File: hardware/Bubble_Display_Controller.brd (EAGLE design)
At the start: 38.1 x 43.2 mm, 33 parts, among them J1 ICSP, Q10 IRFML8244, Q11 IRFML8244, Q12 IRFML8244, Q13 IRFML8244, Q14 IRFML8244, Q15 IRFML8244, Q16 IRFML8244, Q9 IRFML8244, U4 ATMEGA328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

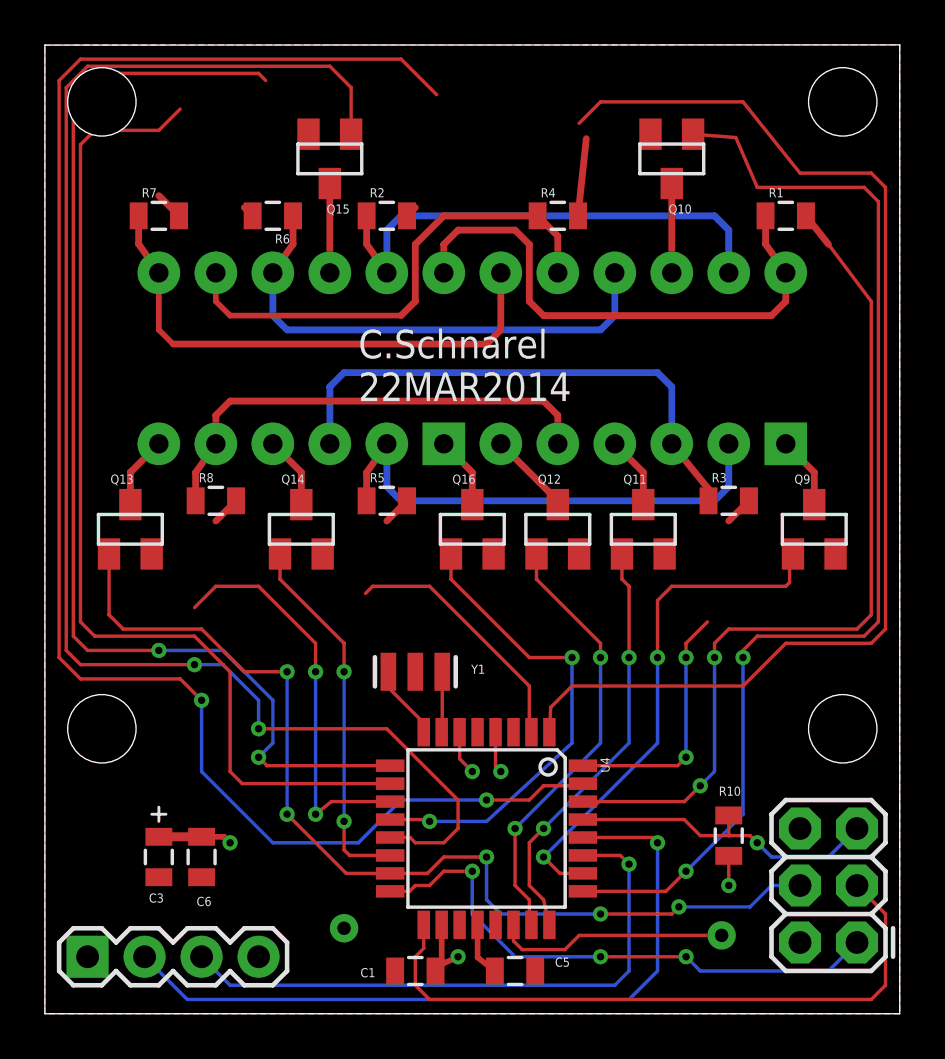
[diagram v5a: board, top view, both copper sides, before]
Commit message: Ordered new board, 8Jyd7Mea. Updating docs to match.
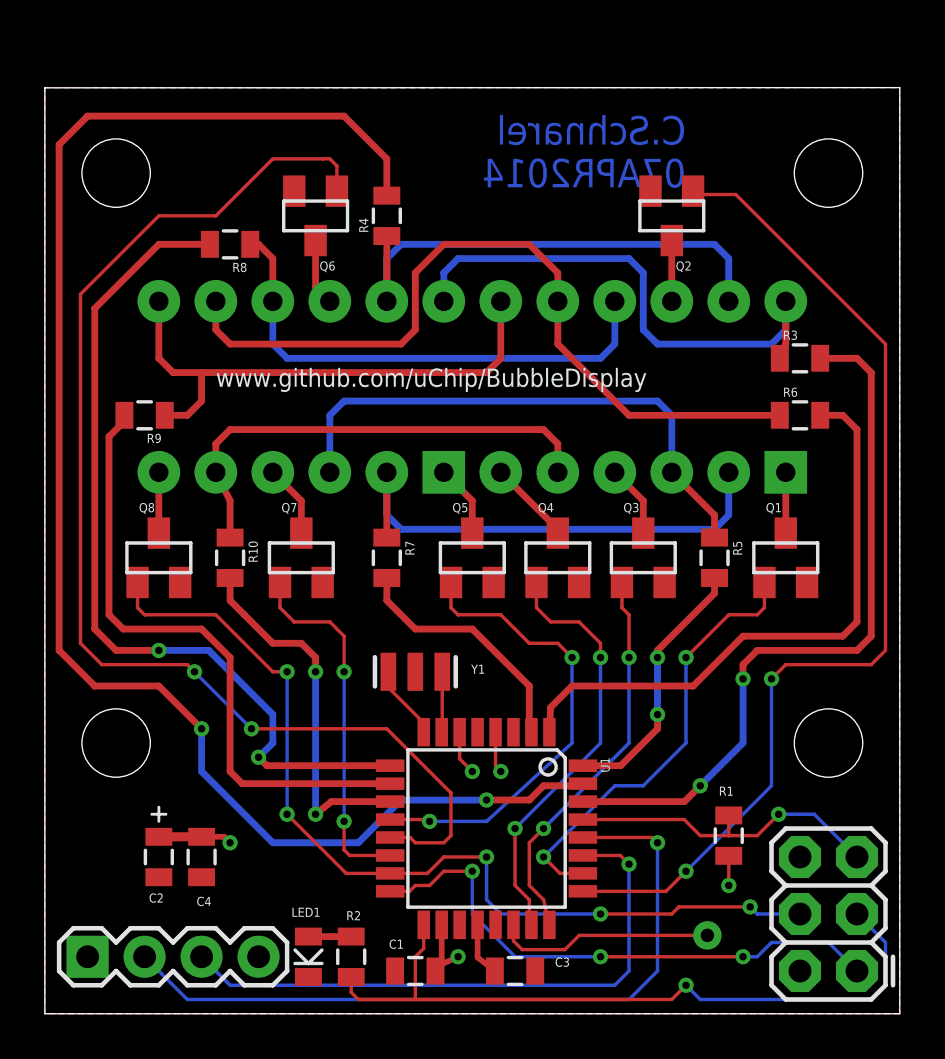
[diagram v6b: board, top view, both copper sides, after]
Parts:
- removed C5: 0.1uF, SparkFun-Capacitors:0805
- removed JP3: BREADBD_VIA, ChipsParts:BBD-VIA
- removed Q10, Q11, Q12, Q13, Q14, Q15, Q16, Q9: IRFML8244, SparkFun-DiscreteSemi:SOT23
- added C2: 10uF, ChipsParts:0805-POL
- added LED1: Amber, ChipsParts:0805-LED
- added Q1, Q2, Q3, Q4, Q5, Q6, Q7, Q8: IRFML8244, SparkFun-DiscreteSemi:SOT23
- added R9: 75, SparkFun-Resistors:0805
- C3: value 10uF -> 0.1uF; device ChipsParts:0805-POL -> SparkFun-Capacitors:0805
- R1: value 75 -> 10k
- R10: value 10k -> 75
- R2: value 75 -> 1k
- moved R2 33.1 mm to (13.7, 2.54), turned to 90 degrees
- moved R1 27.7 mm to (30.5, 7.94), turned to 270 degrees
- moved R10 25.4 mm to (8.26, 20.3)
- moved R6 25.1 mm to (33.7, 26.7), turned to 0 degrees
- moved R7 18.3 mm to (15.2, 20.3), turned to 270 degrees
- moved C3 16.7 mm to (21.0, 1.91), turned to 0 degrees
- moved JP2 16.2 mm to (29.5, 3.49)
- moved R5 14.8 mm to (29.8, 20.3), turned to 270 degrees
- moved R8 11.4 mm to (8.26, 34.3), turned to 180 degrees
- moved R4 7.62 mm to (15.2, 35.6), turned to 90 degrees
- moved R3 7.10 mm to (33.7, 29.2)
- moved U$6 3.24 mm to (34.9, 37.5)
- moved U$5 3.24 mm to (3.17, 37.5)
- moved J1 1.27 mm to (36.2, 1.91)
- moved DISPLAY1 1.27 mm to (26.7, 27.9)
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- renumbered C6 to C4, U4 to U1
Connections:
- removed net EE1: JP2.P$1, U1.19
- removed net EE2: JP3.P$1, U1.22
- new net EE: JP2.P$1, U1.22
- new net N$1: LED1.A, R2.2
- net 5V: now also C2.1, R1.2; no longer C3.1, R10.2
- net A: now also R3.2; no longer R1.2
- net AREF: now also C3.1; no longer C5.1
- net B: now also R4.2; no longer R2.2
- net C: now also R5.2; no longer R3.2
- net CATH1: now also Q1.3; no longer Q9.3
- net CATH2: now also Q2.3; no longer Q10.3
- net CATH3: now also Q3.3; no longer Q11.3
- net CATH4: now also Q4.3; no longer Q12.3
- net CATH5: now also Q5.3; no longer Q16.3
- net CATH6: now also Q6.3; no longer Q15.3
- net CATH7: now also Q7.3; no longer Q14.3
- net CATH8: now also Q8.3; no longer Q13.3
- net D: now also R6.2; no longer R4.2
- net DIG1: now also Q1.1; no longer Q9.1
- net DIG2: now also Q2.1; no longer Q10.1
- net DIG3: now also Q3.1; no longer Q11.1
- net DIG4: now also Q4.1; no longer Q12.1
- net DIG5: now also Q5.1; no longer Q16.1
- net DIG6: now also Q6.1; no longer Q15.1
- net DIG7: now also Q7.1; no longer Q14.1
- net DP: now also R10.2; no longer R8.2
- net E: now also R7.2; no longer R5.2
- net F: now also R8.2; no longer R6.2
- net G: now also R9.2; no longer R7.2
- net GND: now also C2.2, LED1.C, Q1.2, Q2.2, Q3.2, Q4.2, Q5.2, Q6.2, Q7.2, Q8.2; no longer C5.2, Q10.2, Q11.2, Q12.2, Q13.2, Q14.2, Q15.2, Q16.2, Q9.2
- net MOSI/DIG8: now also Q8.1; no longer Q13.1
- net RESET: now also R1.1; no longer R10.1
- net SCK: now also R2.1
- net SEGA: now also R3.1; no longer R1.1
- net SEGB: now also R4.1; no longer R2.1
- net SEGC: now also R5.1; no longer R3.1
- net SEGD: now also R6.1; no longer R4.1
- net SEGDP: now also R10.1; no longer R8.1
- net SEGE: now also R7.1; no longer R5.1
- net SEGF: now also R8.1; no longer R6.1
- net SEGG: now also R9.1; no longer R7.1
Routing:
- net D: track 56.5 -> 26.8 mm
- net G: track 47.0 -> 27.8 mm
- net F: track 52.6 -> 38.3 mm
- net SEGD: track 22.1 -> 35.0 mm
- net DIG6: track 66.3 -> 54.8 mm
- net EE2: track 10.4 -> 0.00 mm
- net EE: track 0.00 -> 9.78 mm
- net A: track 38.4 -> 32.2 mm
- net DIG2: track 51.1 -> 45.8 mm
- net B: track 73.8 -> 69.2 mm
- net SCK: track 29.3 -> 32.8 mm, vias 0 -> 1
- net DIG1: track 23.2 -> 19.9 mm
- net MOSI/DIG8: track 45.0 -> 42.0 mm
- net DP: track 19.3 -> 16.4 mm
- net N$1: track 0.00 -> 1.90 mm
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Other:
- board size 38.1 x 43.2 mm -> 38.1 x 41.3 mm
- board text added: "C.Schnarel 07APR2014"
- board text added: "www.github.com/uChip/BubbleDisplay"
- board text removed: "C.Schnarel 22MAR2014"
